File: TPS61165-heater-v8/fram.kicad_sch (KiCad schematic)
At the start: 2 parts

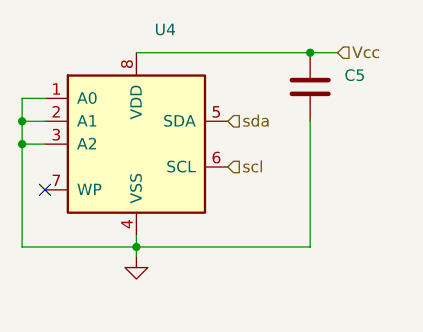
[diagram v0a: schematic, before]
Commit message: commit updates to high power heater
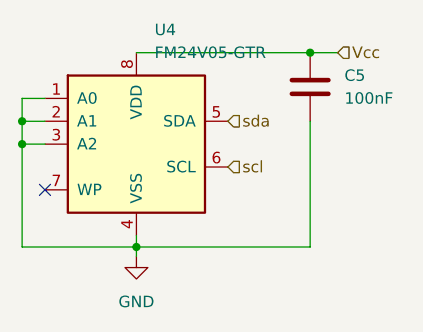
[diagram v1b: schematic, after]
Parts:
- C5: value (none) -> 100nF; footprint (none) -> Capacitor_SMD:C_0603_1608Metric_Pad1.08x0.95mm_HandSolder
- U4: value (none) -> FM24V05-GTR; footprint (none) -> Package_SO:SOIC-8_3.9x4.9mm_P1.27mm
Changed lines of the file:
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@@
       (effects (font (size 1.27 1.27)) (justify left))
     )
-    (property "Value" "" (id 1) (at 152.8954 80.01 0)
+    (property "Value" "FM24V05-GTR" (id 1) (at 152.8954 80.01 0)
       (effects (font (size 1.27 1.27)) (justify left))
     )
-    (property "Footprint" "" (id 2) (at 150.876 90.17 0)
+    (property "Footprint" "Package_SO:SOIC-8_3.9x4.9mm_P1.27mm" (id 2) (at 150.876 90.17 0)
       (effects (font (size 1.27 1.27)) hide)
     )
@@
       (effects (font (size 1.27 1.27)) (justify left))
     )
-    (property "Value" "" (id 1) (at 173.99 85.0899 0)
+    (property "Value" "100nF" (id 1) (at 173.99 85.0899 0)
       (effects (font (size 1.27 1.27)) (justify left))
     )
-    (property "Footprint" "" (id 2) (at 171.1452 87.63 0)
+    (property "Footprint" "Capacitor_SMD:C_0603_1608Metric_Pad1.08x0.95mm_HandSolder" (id 2) (at 171.1452 87.63 0)
       (effects (font (size 1.27 1.27)) hide)
     )
@@
       (effects (font (size 1.27 1.27)) hide)
     )
-    (property "Value" "" (id 1) (at 150.876 107.696 0))
+    (property "Value" "GND" (id 1) (at 150.876 107.696 0))
     (property "Footprint" "" (id 2) (at 150.876 102.616 0)
       (effects (font (size 1.27 1.27)) hide)
